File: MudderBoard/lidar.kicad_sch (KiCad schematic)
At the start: 24 parts, among them M1 NMOS, M2 NMOS, U1 LM5122QMH/NOPB

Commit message: Layout
Pixhawk and Lidar
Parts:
- R5: footprint Lidar_Foot:RESC3015X65N -> Resistor_SMD:R_1206_3216Metric_Pad1.30x1.75mm_HandSolder
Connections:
- no-connect marks 0 -> 1
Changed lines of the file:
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@@
 		(color 0 0 0 0)
+	)
+	(no_connect
+		(at 102.87 102.87)
 	)
 	(wire
@@
 			)
 		)
-		(property "Footprint" "Lidar_Foot:RESC3015X65N"
+		(property "Footprint" "Resistor_SMD:R_1206_3216Metric_Pad1.30x1.75mm_HandSolder"
 			(at 91.694 48.514 90)
 			(effects

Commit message: Schematic updates
global labels and test points
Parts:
- added TP39, TP40, TP41: TestPoint, TestPoint:TestPoint_Pad_1.0x1.0mm, symbol Connector:TestPoint
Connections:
- net +24V: now also TP40.1
- net +BATT: now also TP39.1
- net at C7.2, C8.2, R8.2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: now also TP41.1
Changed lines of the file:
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@@
-	(wire
-		(pts
-			(xy 271.78 43.18) (xy 271.78 49.53)
-		)
-		(stroke
-			(width 0)
-			(type default)
-		)
-	)
 	(wire
 		(pts
@@
 		)
 	)
-	(label "+24V"
-		(at 271.78 43.18 0)
+	(global_label "+24V"
+		(shape input)
+		(at 271.78 49.53 0)
 		(fields_autoplaced yes)
 		(effects
@@
 				(size 1.27 1.27)
 			)
-			(justify left bottom)
+			(justify left)
+		)
+		(property "Intersheetrefs" "${INTERSHEET_REFS}"
+			(at 279.8452 49.53 0)
+			(effects
+				(font
+					(size 1.27 1.27)
+				)
+				(justify left)
+				(hide yes)
+			)
+		)
+	)
+	(symbol
+		(lib_id "Connector:TestPoint")
+		(at 30.48 49.53 0)
+		(unit 1)
+		(exclude_from_sim no)
+		(in_bom yes)
+		(on_board yes)
+		(dnp no)
+		(fields_autoplaced yes)
+		(property "Reference" "TP39"
+			(at 33.02 44.9579 0)
+			(effects
+				(font
+					(size 1.27 1.27)
+				)
+				(justify left)
+			)
+		)
+		(property "Value" "TestPoint"
+			(at 33.02 47.4979 0)
+			(effects
+				(font
+					(size 1.27 1.27)
+				)
+				(justify left)
+			)
+		)
+		(property "Footprint" "TestPoint:TestPoint_Pad_1.0x1.0mm"
+			(at 35.56 49.53 0)
+			(effects
+				(font
+					(size 1.27 1.27)
+				)
+				(hide yes)
+			)
+		)
+		(property "Datasheet" "~"
+			(at 35.56 49.53 0)
+			(effects
+				(font
+					(size 1.27 1.27)
+				)
+				(hide yes)
+			)
+		)
+		(property "Description" "test point"
+			(at 30.48 49.53 0)
+			(effects
+				(font
+					(size 1.27 1.27)
+				)
+				(hide yes)
+			)
+		)
+		(pin "1"
+		)
+		(instances
+			(project ""
+				(path "/cdf98bf7-80ce-4b13-b655-e6c7c589c122/86bd7edb-9c3d-421e-84f7-984954447f61"
+					(reference "TP39")
+					(unit 1)
+				)
+			)
 		)
 	)
@@
 	)
 	(symbol
+		(lib_id "Connector:TestPoint")
+		(at 267.97 49.53 0)
+		(unit 1)
+		(exclude_from_sim no)
+		(in_bom yes)
+		(on_board yes)
+		(dnp no)
+		(property "Reference" "TP40"
+			(at 257.556 44.196 0)
+			(effects
+				(font
+					(size 1.27 1.27)
+				)
+				(justify left)
+			)
+		)
+		(property "Value" "TestPoint"
+			(at 257.556 46.482 0)
+			(effects
+				(font
+					(size 1.27 1.27)
+				)
+				(justify left)
+			)
+		)
+		(property "Footprint" "TestPoint:TestPoint_Pad_1.0x1.0mm"
+			(at 273.05 49.53 0)
+			(effects
+				(font
+					(size 1.27 1.27)
+				)
+				(hide yes)
+			)
+		)
+		(property "Datasheet" "~"
+			(at 273.05 49.53 0)
+			(effects
+				(font
+					(size 1.27 1.27)
+				)
+				(hide yes)
+			)
+		)
+		(property "Description" "test point"
+			(at 267.97 49.53 0)
+			(effects
+				(font
+					(size 1.27 1.27)
+				)
+				(hide yes)
+			)
+		)
+		(pin "1"
+		)
+		(instances
+			(project "MudderBoard"
+				(path "/cdf98bf7-80ce-4b13-b655-e6c7c589c122/86bd7edb-9c3d-421e-84f7-984954447f61"
+					(reference "TP40")
+					(unit 1)
+				)
+			)
+		)
+	)
+	(symbol
 		(lib_id "Device:R_US")
 		(at 203.2 87.63 270)
@@
 					(unit 1)
 				)
+			)
+		)
+	)
+	(symbol
+		(lib_id "Connector:TestPoint")
+		(at 233.68 92.71 270)
+		(unit 1)
+		(exclude_from_sim no)
+		(in_bom yes)
+		(on_board yes)
+		(dnp no)
+		(fields_autoplaced yes)
+		(property "Reference" "TP41"
+			(at 238.76 91.4399 90)
+			(effects
+				(font
+					(size 1.27 1.27)
+				)
+				(justify left)
+			)
+		)
+		(property "Value" "TestPoint"
+			(at 238.76 93.9799 90)
+			(effects
+				(font
+					(size 1.27 1.27)
+				)
+				(justify left)
+			)
+		)
+		(property "Footprint" "TestPoint:TestPoint_Pad_1.0x1.0mm"
+			(at 233.68 97.79 0)
+			(effects
+				(font
+					(size 1.27 1.27)
+				)
+				(hide yes)
+			)
+		)
+		(property "Datasheet" "~"
+			(at 233.68 97.79 0)
+			(effects
+				(font
+					(size 1.27 1.27)
+				)
+				(hide yes)
+			)
+		)
+		(property "Description" "test point"
+			(at 233.68 92.71 0)
+			(effects
+				(font
+					(size 1.27 1.27)
+				)
+				(hide yes)
+			)
+		)
+		(pin "1"
+		)
+		(instances
+			(project "MudderBoard"
+				(path "/cdf98bf7-80ce-4b13-b655-e6c7c589c122/86bd7edb-9c3d-421e-84f7-984954447f61"
+					(reference "TP41")
+					(unit 1)
+				)

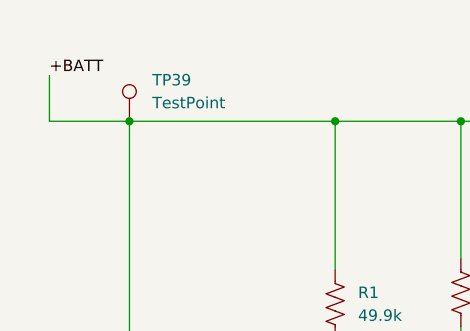
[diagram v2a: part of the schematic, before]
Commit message: Schematic and Layout
TPs and net labels
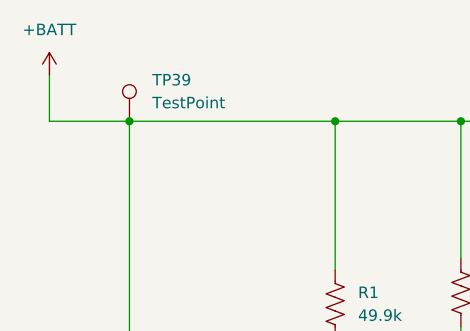
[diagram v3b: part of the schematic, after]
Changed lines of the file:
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@@
 		)
 	)
-	(label "+BATT"
-		(at 21.59 44.45 0)
+	(global_label "+24V"
+		(shape input)
+		(at 271.78 49.53 0)
 		(fields_autoplaced yes)
 		(effects
@@
 				(size 1.27 1.27)
 			)
-			(justify left bottom)
-		)
-	)
-	(global_label "+24V"
-		(shape input)
-		(at 271.78 49.53 0)
-		(fields_autoplaced yes)
-		(effects
-			(font
-				(size 1.27 1.27)
-			)
 			(justify left)
 		)
@@
 					(unit 1)
 				)
+			)
+		)
+	)
+	(symbol
+		(lib_id "power:+BATT")
+		(at 21.59 44.45 0)
+		(unit 1)
+		(exclude_from_sim no)
+		(in_bom yes)
+		(on_board yes)
+		(dnp no)
+		(fields_autoplaced yes)
+		(property "Reference" "#PWR037"
+			(at 21.59 48.26 0)
+			(effects
+				(font
+					(size 1.27 1.27)
+				)
+				(hide yes)
+			)
+		)
+		(property "Value" "+BATT"
+			(at 21.59 39.37 0)
+			(effects
+				(font
+					(size 1.27 1.27)
+				)
+			)
+		)
+		(property "Footprint" ""
+			(at 21.59 44.45 0)
+			(effects
+				(font
+					(size 1.27 1.27)
+				)
+				(hide yes)
+			)
+		)
+		(property "Datasheet" ""
+			(at 21.59 44.45 0)
+			(effects
+				(font
+					(size 1.27 1.27)
+				)
+				(hide yes)
+			)
+		)
+		(property "Description" "Power symbol creates a global label with name \"+BATT\""
+			(at 21.59 44.45 0)
+			(effects
+				(font
+					(size 1.27 1.27)
+				)
+				(hide yes)
+			)
+		)
+		(pin "1"
+		)
+		(instances
+			(project ""
+				(path "/cdf98bf7-80ce-4b13-b655-e6c7c589c122/86bd7edb-9c3d-421e-84f7-984954447f61"
+					(reference "#PWR037")
+					(unit 1)
+				)
